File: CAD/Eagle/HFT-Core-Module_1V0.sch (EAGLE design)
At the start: 399 parts, among them Q0521 ABS07-32.768KHZ, Q0811 ABM03B-32.000MHZ, Q0911 ABM3B-16MHZ-10-R50-1-U, T1201 MMBT2222, T1202 MMBT2222, T1203 MMBT2222, U0111 STM32L4Z_144PIN_SMPS, U0431 PAM2305AAB120, U0601 LM4120IM5-3.0, U0611 MAX5217, U0631 CFPT-141-20MHZ, U0641 OPA354, U0701 Si5338, U0801 SX1276, U0901 AX5243, U0911 PE4259, U0921 PE4259, U0991 PE4259, U1101 MCP3911A0-E-SS, U1111 MAX5136AGTG+, U1121 OPA354, U1131 OPA354, U1141 OPA354, U1201 NHD-C0220BIZ_2X20CHARS, U1301 MPU-9250, U1311 MS5607-02BA03, U1321 SHT31-DIS, U1401 SOLARPANEL_3V3_5MA1_25MM_X_20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, U1402 SPV1040T, U1501 TS5A23166, U1601 PAM2305AAB330, U1701 TS5A23166, U1801 TS5A23166, U1901 TS5A23166, X1261 TTE_EN11-HSM, X2001 MOLEX 105017-0001, X2101 SMA_SMT_AMPHENOL-901-143, X2111 SMA_SMT_AMPHENOL-901-143, X2201 CUI SJ1-3535NS, X2211 CUI SJ1-3535NS, X2311 2X20/90_1MM27_HARWIN_M50-3202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, X2312 2X20/90_1MM27_HARWIN_M50-3202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, X2321 2X20/90_1MM27_HARWIN_M50-3202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, X2322 2X20/90_1MM27_HARWIN_M50-3202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, X2331 2X20/90_1MM27_HARWIN_M50-3202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, X2332 2X20/90_1MM27_HARWIN_M50-3202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

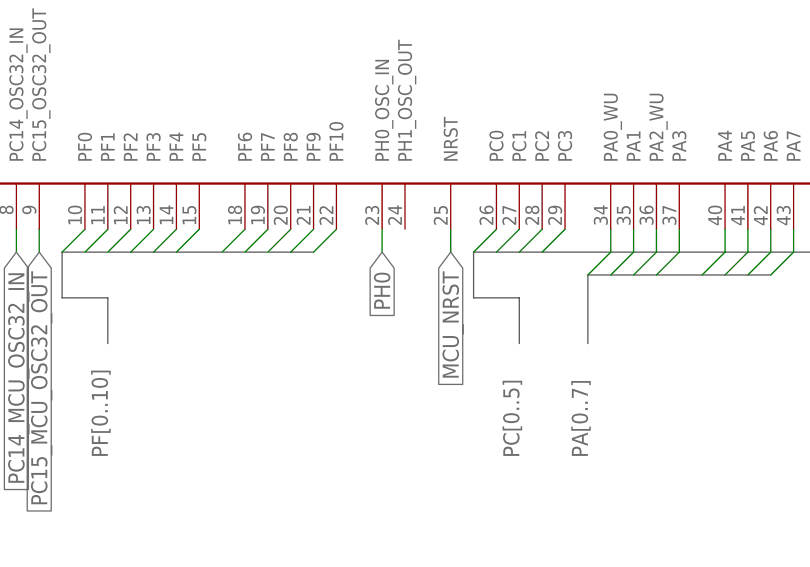
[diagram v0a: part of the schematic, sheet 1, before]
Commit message: HW_1V0 - routing for LQFP144 package fixed and minor other fixes
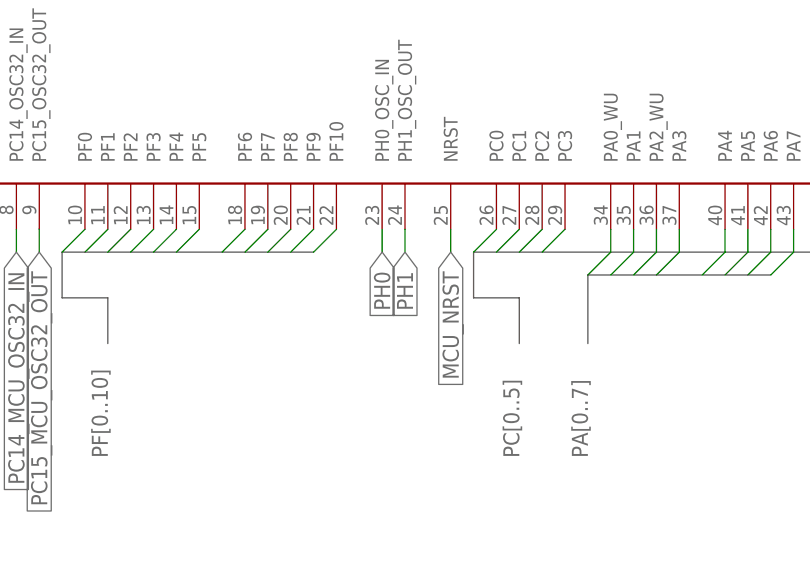
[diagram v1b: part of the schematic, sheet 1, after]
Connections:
- new net PH1: U0111.PH1_OSC_OUT
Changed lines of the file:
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@@
+</segment>
+</net>
+<net name="PH1" class="0">
+<segment>
+<pinref part="U0111" gate="G$1" pin="PH1_OSC_OUT"/>
+<wire x1="114.3" y1="38.1" x2="114.3" y2="35.56" width="0.1524" layer="91"/>
+<label x="114.3" y="35.56" size="1.778" layer="95" rot="R270" xref="yes"/>
 </segment>
 </net>

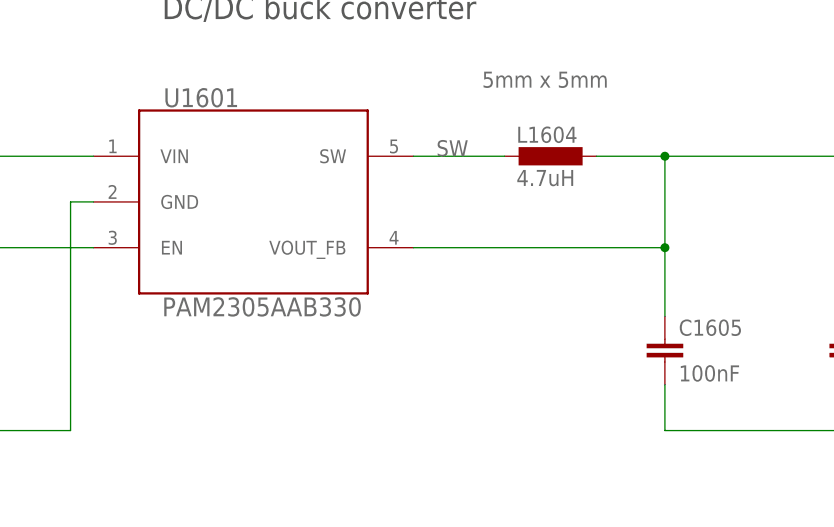
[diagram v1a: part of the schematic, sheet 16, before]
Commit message: HW_1V0 - outdated DC/DC buck converter replaced
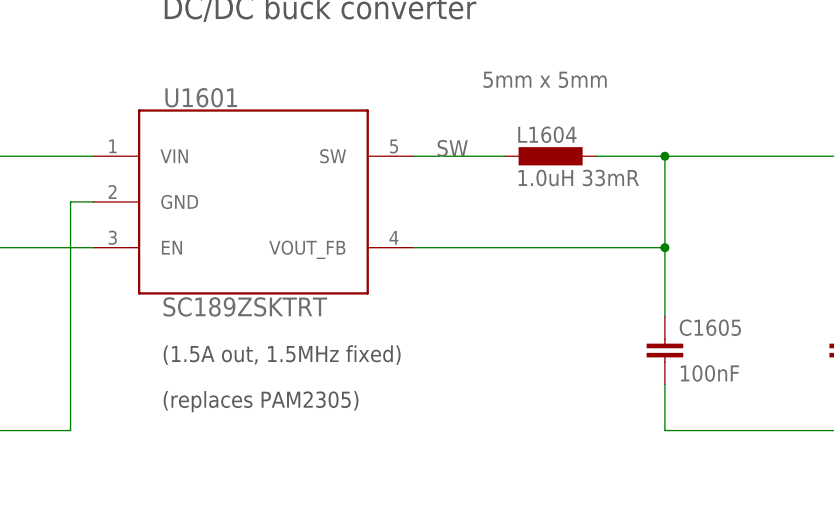
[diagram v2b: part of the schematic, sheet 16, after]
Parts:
- L0433: value 2.2uH -> 2.2uH 14mR
- L1604: value 4.7uH -> 1.0uH 33mR
- U1601: value PAM2305AAB330 -> SC189ZSKTRT
- X2101, X2111: value SMA_SMT_AMPHENOL-901-143 -> SMA_SMT_AMPHENOL-901-143, SAMTEC SMA-J-P-H-RA-TH1
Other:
- note added: "(1.0A out, 1.5MHz fixed)"
- note added: "(1.5A out, 1.5MHz fixed)"
- note added: "(replaces PAM2305)"
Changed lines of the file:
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@@
 <part name="X2331" library="df4iah_connector" deviceset="2X20/90_1MM27_HARWIN_M50-3202045" device=""/>
 <part name="C1602" library="rcl" deviceset="C-EU" device="C0805" value="47uF"/>
-<part name="L1604" library="rcl" deviceset="L-EU" device="L5650M" value="4.7uH"/>
+<part name="L1604" library="rcl" deviceset="L-EU" device="L5650M" value="1.0uH 33mR"/>
 <part name="C1605" library="rcl" deviceset="C-EU" device="C0603" value="100nF"/>
 <part name="C1606" library="rcl" deviceset="C-EU" device="C0805" value="47uF"/>
@@
 <part name="GND0431" library="df4iah_supply" deviceset="GND" device=""/>
 <part name="C0444" library="rcl" deviceset="C-EU" device="C0805" value="10uF"/>
-<part name="L0433" library="df4iah_rcl" deviceset="L-EU" device="6.0X6.0MM" value="2.2uH"/>
+<part name="L0433" library="df4iah_rcl" deviceset="L-EU" device="6.0X6.0MM" value="2.2uH 14mR"/>
 <part name="U0901" library="df4iah_rf" deviceset="AX5243" device=""/>
 <part name="D1403" library="df4iah_diode" deviceset="CRS08" device=""/>
@@
 <part name="X2332" library="df4iah_connector" deviceset="2X20/90_1MM27_HARWIN_M50-3202045" device=""/>
 <part name="S0312" library="df4iah_switch" deviceset="KSR223G_SMD_1POL" device="" value="KSR223G"/>
-<part name="U1601" library="df4iah_powersupply" deviceset="PAM2305" device="" value="PAM2305AAB330"/>
+<part name="U1601" library="df4iah_powersupply" deviceset="PAM2305" device="" value="SC189ZSKTRT"/>
 <part name="U1402" library="df4iah_powersupply" deviceset="SPV1040" device="" value="SPV1040T"/>
 <part name="R2002" library="rcl" deviceset="R-EU_" device="R0603" value="330kR"/>
@@
 <part name="R1104" library="rcl" deviceset="R-EU_" device="R0603" value="22kR"/>
 <part name="R1105" library="rcl" deviceset="R-EU_" device="R0603" value="22kR"/>
-<part name="X2101" library="df4iah_connector" deviceset="SMA_SMT_AMPHENOL-901-143" device=""/>
-<part name="X2111" library="df4iah_connector" deviceset="SMA_SMT_AMPHENOL-901-143" device=""/>
+<part name="X2101" library="df4iah_connector" deviceset="SMA_SMT_AMPHENOL-901-143" device="" value="SMA_SMT_AMPHENOL-901-143, SAMTEC SMA-J-P-H-RA-TH1"/>
+<part name="X2111" library="df4iah_connector" deviceset="SMA_SMT_AMPHENOL-901-143" device="" value="SMA_SMT_AMPHENOL-901-143, SAMTEC SMA-J-P-H-RA-TH1"/>
 <part name="TP_AX_TCXO_EN" library="testpad" deviceset="PTR1" device="TP06R"/>
 <part name="TP_AX_IRQ" library="testpad" deviceset="PTR1" device="TP06R"/>
@@
 <text x="165.1" y="73.66" size="2.54" layer="97" ratio="15">MCU VBAT</text>
 <text x="180.34" y="78.74" size="1.778" layer="97">not needed!</text>
+<text x="48.26" y="15.24" size="1.778" layer="97">(1.0A out, 1.5MHz fixed)</text>
 </plain>
 <instances>
@@
 <text x="104.14" y="111.76" size="2.54" layer="97" ratio="15">DC/DC buck converter</text>
 <text x="22.86" y="162.56" size="2.54" layer="97" ratio="15">Power converter 5V --&gt; 3.3V</text>
+<text x="104.14" y="73.66" size="1.778" layer="97">(1.5A out, 1.5MHz fixed)</text>
+<text x="104.14" y="68.58" size="1.778" layer="97">(replaces PAM2305)</text>
 </plain>
 <instances>

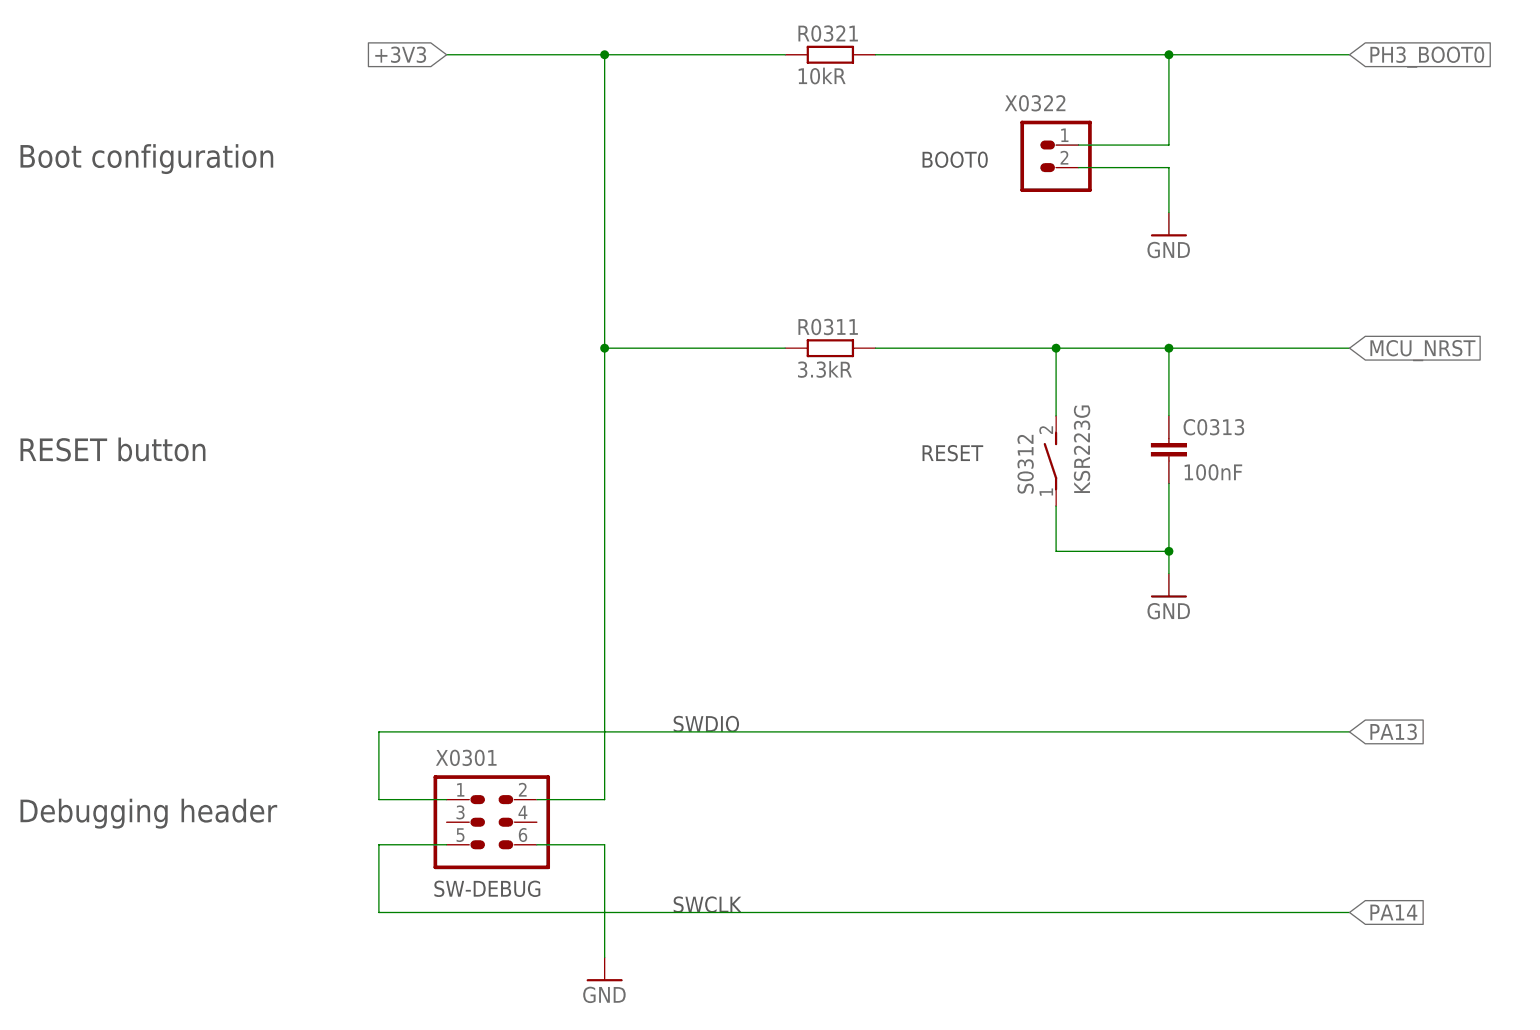
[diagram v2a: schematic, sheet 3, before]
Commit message: HW_1V0 - SWD header, XO 32.768kHz caps, RESET resistor removed
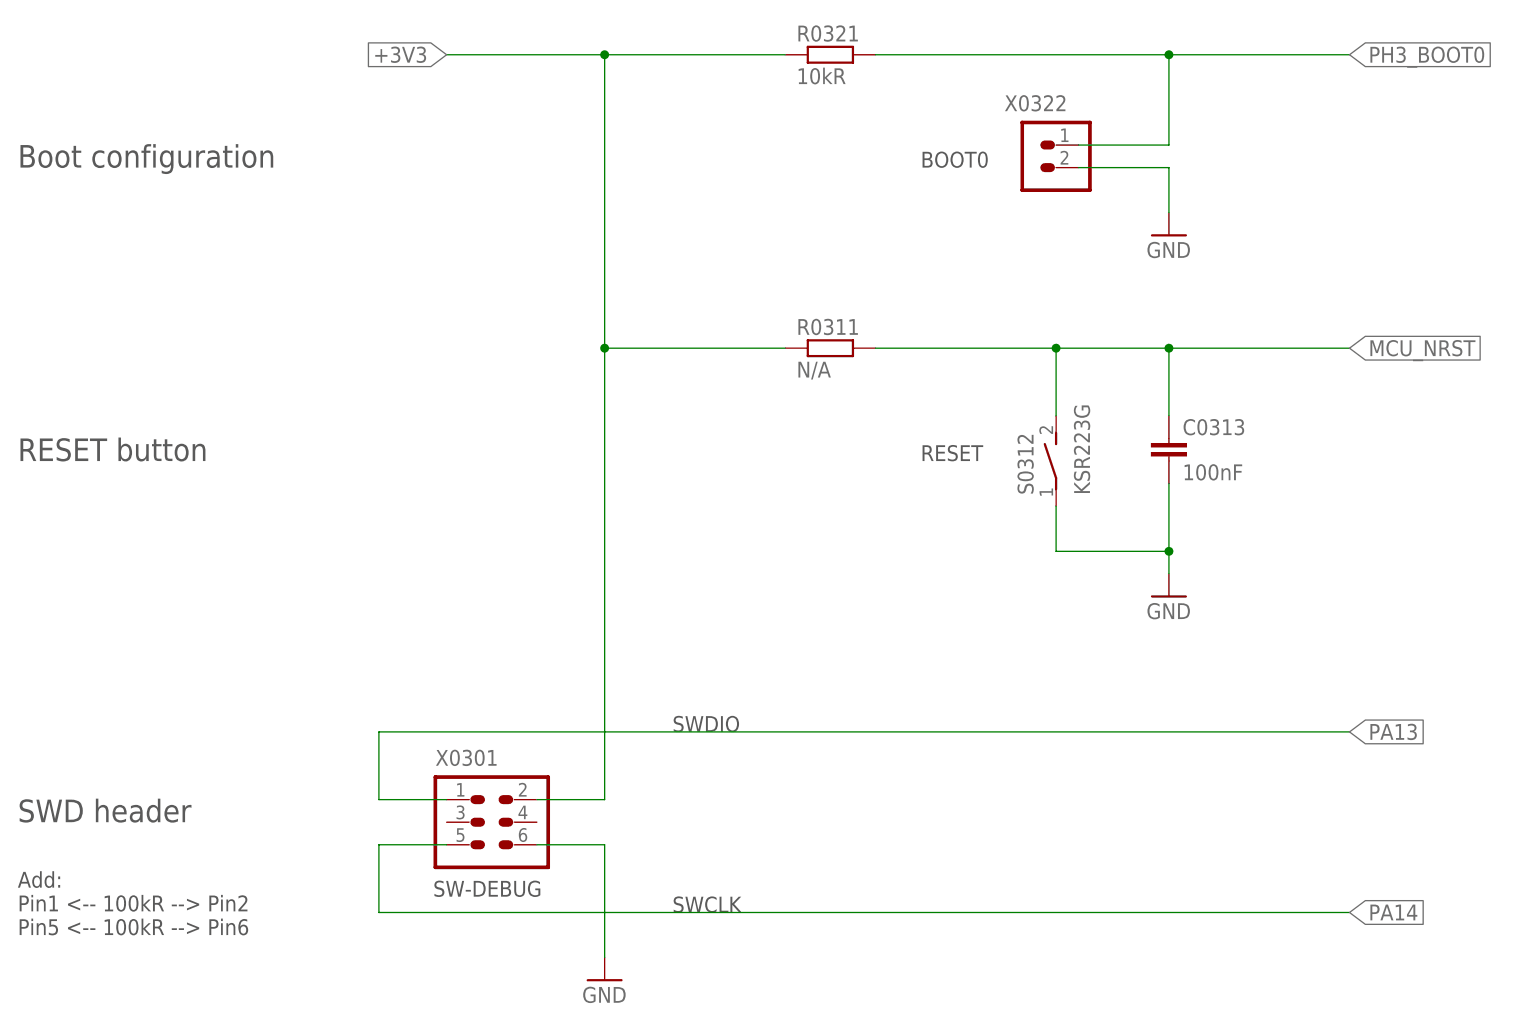
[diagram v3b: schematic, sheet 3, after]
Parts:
- C0511: value 1.5pF -> 22pF
- R0311: value 3.3kR -> N/A
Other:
- note added: "Add: Pin1 <-- 100kR --> Pin2 Pin5 <-- 100kR --> Pin6"
- note added: "SWD header"
- note removed: "Debugging header"
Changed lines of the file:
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@@
 <part name="R0321" library="rcl" deviceset="R-EU_" device="R0603" value="10kR"/>
 <part name="C0313" library="rcl" deviceset="C-EU" device="C0603" value="100nF"/>
-<part name="R0311" library="rcl" deviceset="R-EU_" device="R0603" value="3.3kR"/>
+<part name="R0311" library="rcl" deviceset="R-EU_" device="R0603" value="N/A"/>
 <part name="GND0311" library="df4iah_supply" deviceset="GND" device=""/>
 <part name="FRAME_14" library="df4iah_frame" deviceset="A4L-LOC" device="" value="I2C connector"/>
@@
 <part name="FRAME_05" library="df4iah_frame" deviceset="A4L-LOC" device="" value="I2C connector"/>
 <part name="Q0521" library="df4iah_crystal" deviceset="ABS07-32.768KHZ" device=""/>
-<part name="C0511" library="rcl" deviceset="C-EU" device="C0603" value="1.5pF"/>
+<part name="C0511" library="rcl" deviceset="C-EU" device="C0603" value="22pF"/>
 <part name="GND0511" library="df4iah_supply" deviceset="GND" device=""/>
 <part name="GND0531" library="df4iah_supply" deviceset="GND" device=""/>
@@
 <text x="127" y="137.16" size="1.778" layer="97">BOOT0</text>
 <text x="72.136" y="55.118" size="1.778" layer="97">SW-DEBUG</text>
-<text x="25.4" y="63.5" size="2.54" layer="97" ratio="15">Debugging header</text>
+<text x="25.4" y="63.5" size="2.54" layer="97" ratio="15">SWD header</text>
 <text x="25.4" y="137.16" size="2.54" layer="97" ratio="15">Boot configuration</text>
 <text x="25.4" y="104.14" size="2.54" layer="97" ratio="15">RESET button</text>
+<text x="25.4" y="50.8" size="1.778" layer="97">Add:
+Pin1 &lt;-- 100kR --&gt; Pin2
+Pin5 &lt;-- 100kR --&gt; Pin6</text>
 </plain>
 <instances>

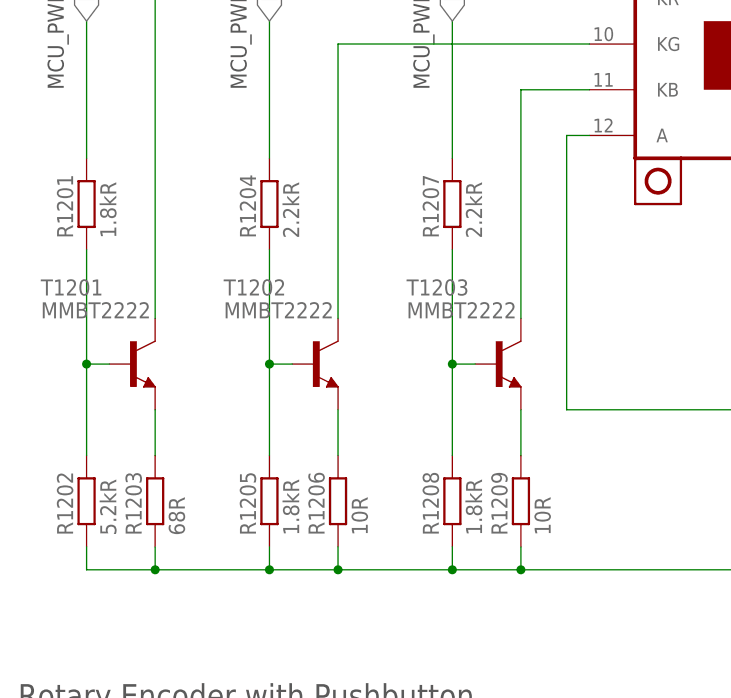
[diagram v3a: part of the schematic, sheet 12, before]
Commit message: HW_1V0 - LCD-backlight resistors changed
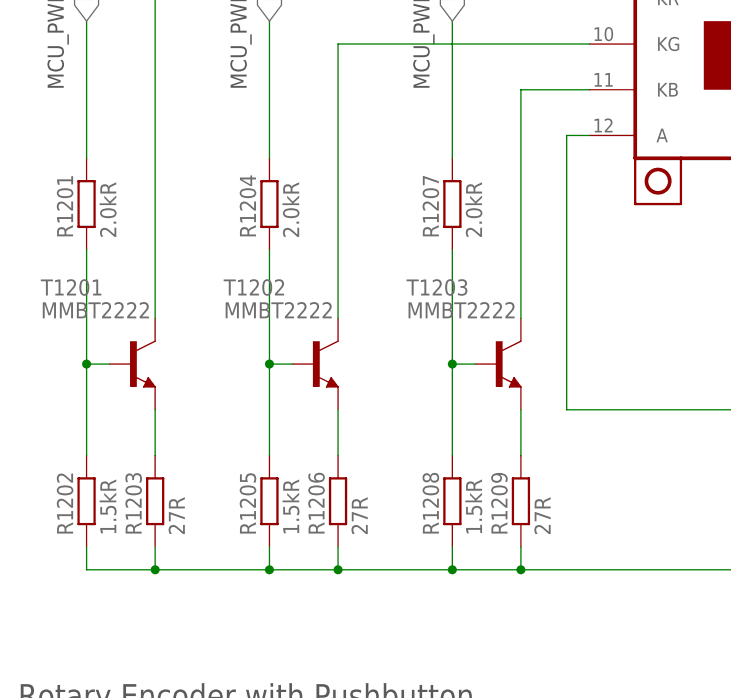
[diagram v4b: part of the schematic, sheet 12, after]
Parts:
- R1201: value 1.8kR -> 2.0kR
- R1202: value 5.2kR -> 1.5kR
- R1203: value 68R -> 27R
- R1204, R1207: value 2.2kR -> 2.0kR
- R1205, R1208: value 1.8kR -> 1.5kR
- R1206, R1209: value 10R -> 27R
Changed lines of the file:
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@@
 <part name="T1202" library="transistor" deviceset="BC846" device="" value="MMBT2222"/>
 <part name="T1203" library="transistor" deviceset="BC846" device="" value="MMBT2222"/>
-<part name="R1209" library="rcl" deviceset="R-EU_" device="R0805" value="10R"/>
-<part name="R1208" library="rcl" deviceset="R-EU_" device="R0603" value="1.8kR"/>
-<part name="R1207" library="rcl" deviceset="R-EU_" device="R0603" value="2.2kR"/>
-<part name="R1206" library="rcl" deviceset="R-EU_" device="R0805" value="10R"/>
-<part name="R1203" library="rcl" deviceset="R-EU_" device="R0805" value="68R"/>
-<part name="R1205" library="rcl" deviceset="R-EU_" device="R0603" value="1.8kR"/>
-<part name="R1202" library="rcl" deviceset="R-EU_" device="R0603" value="5.2kR"/>
-<part name="R1204" library="rcl" deviceset="R-EU_" device="R0603" value="2.2kR"/>
-<part name="R1201" library="rcl" deviceset="R-EU_" device="R0603" value="1.8kR"/>
+<part name="R1209" library="rcl" deviceset="R-EU_" device="R0805" value="27R"/>
+<part name="R1208" library="rcl" deviceset="R-EU_" device="R0603" value="1.5kR"/>
+<part name="R1207" library="rcl" deviceset="R-EU_" device="R0603" value="2.0kR"/>
+<part name="R1206" library="rcl" deviceset="R-EU_" device="R0805" value="27R"/>
+<part name="R1203" library="rcl" deviceset="R-EU_" device="R0805" value="27R"/>
+<part name="R1205" library="rcl" deviceset="R-EU_" device="R0603" value="1.5kR"/>
+<part name="R1202" library="rcl" deviceset="R-EU_" device="R0603" value="1.5kR"/>
+<part name="R1204" library="rcl" deviceset="R-EU_" device="R0603" value="2.0kR"/>
+<part name="R1201" library="rcl" deviceset="R-EU_" device="R0603" value="2.0kR"/>
 <part name="FRAME_13" library="df4iah_frame" deviceset="A4L-LOC" device="" value="Holes"/>
 <part name="U1301" library="df4iah_sensors" deviceset="MPU-9250" device="" value="MPU-9250"/>
